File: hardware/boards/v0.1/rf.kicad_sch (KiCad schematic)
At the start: 12 parts, among them J1 WIFI_JTAG, SW22 BOOT, SW23 RST, U22 nRF, U27 ESP32-S3-MINI-1U, Y2 32.768kHz

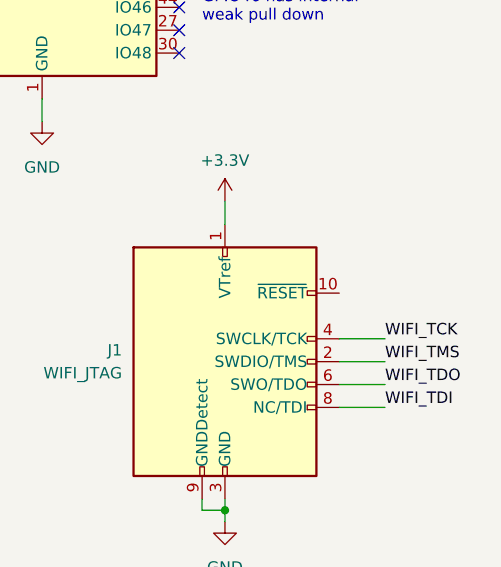
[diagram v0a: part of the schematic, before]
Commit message: feat: more routing and DRC cleanup
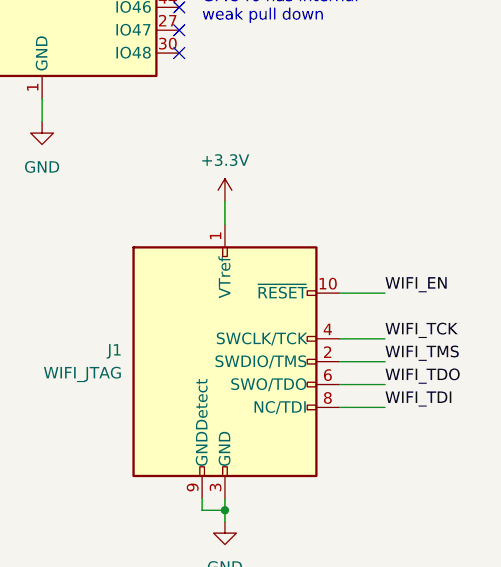
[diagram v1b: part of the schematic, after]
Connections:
- net ~{WIFI_EN}: now also J1.10 (~{RESET})
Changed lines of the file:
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@@
+	(wire
+		(pts
+			(xy 266.7 134.62) (xy 271.78 134.62)
+		)
+		(stroke
+			(width 0)
+			(type default)
+		)
+	)
 	(wire
 		(pts
@@
 		(effects
 			(font
+				(size 1.27 1.27)
+			)
+			(justify left bottom)
+		)
+	)
+	(label "WIFI_EN"
+		(at 271.78 134.62 0)
+		(effects
+			(font

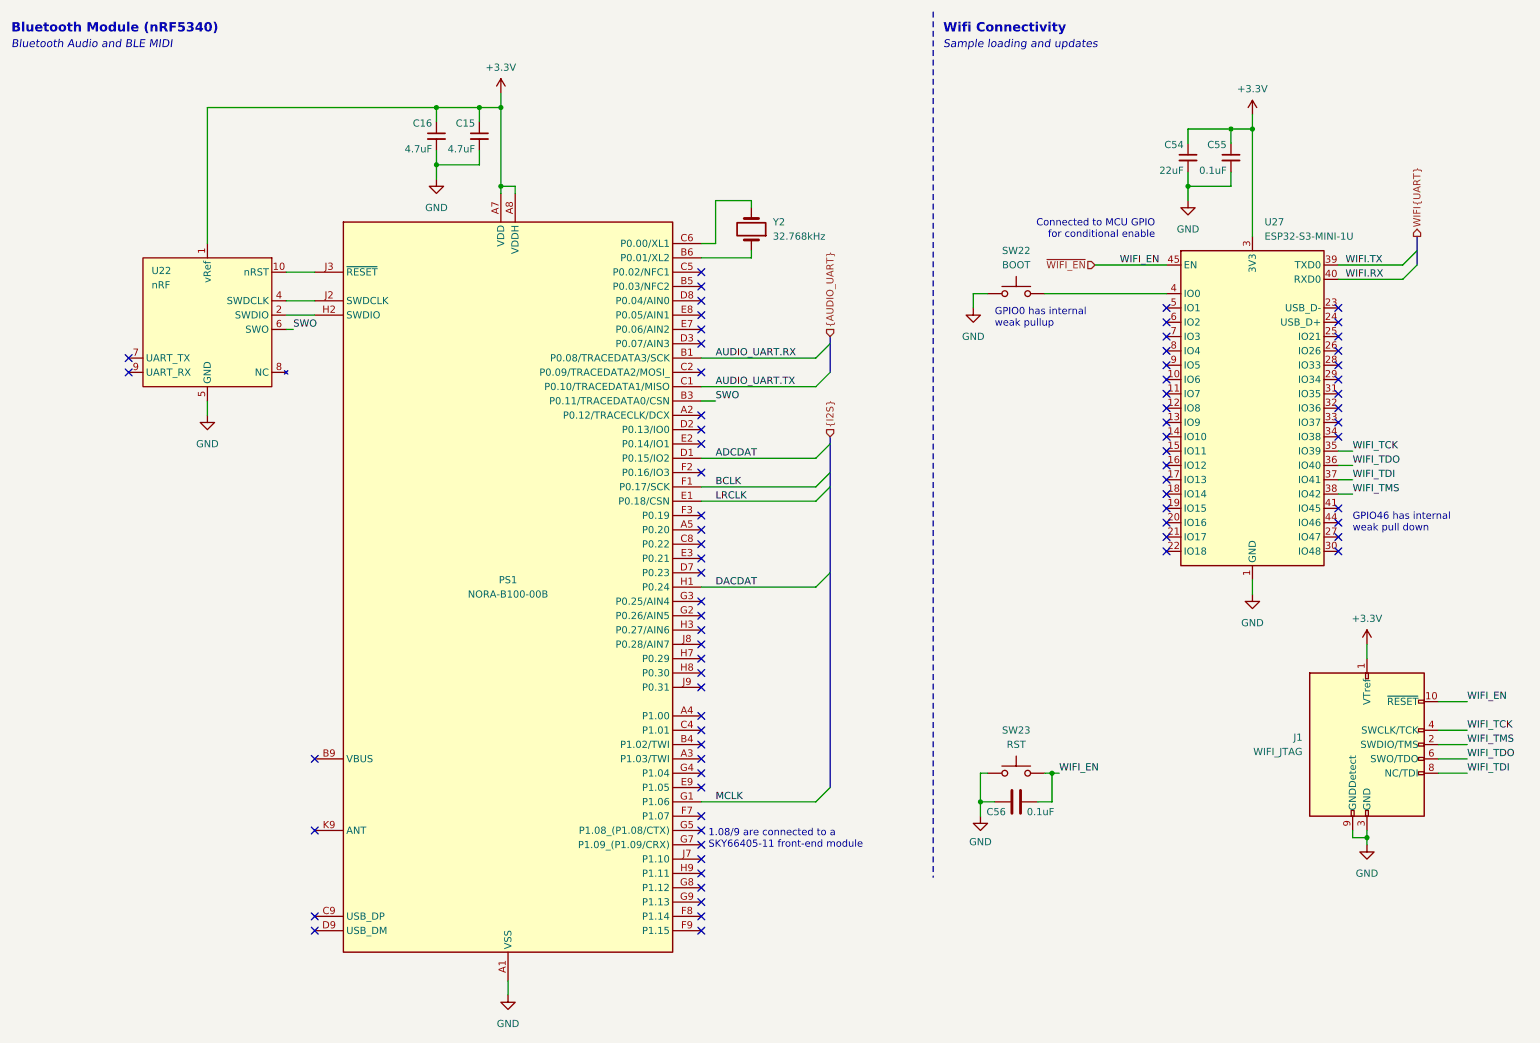
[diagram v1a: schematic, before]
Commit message: feat: clean up routing, remove metronome light
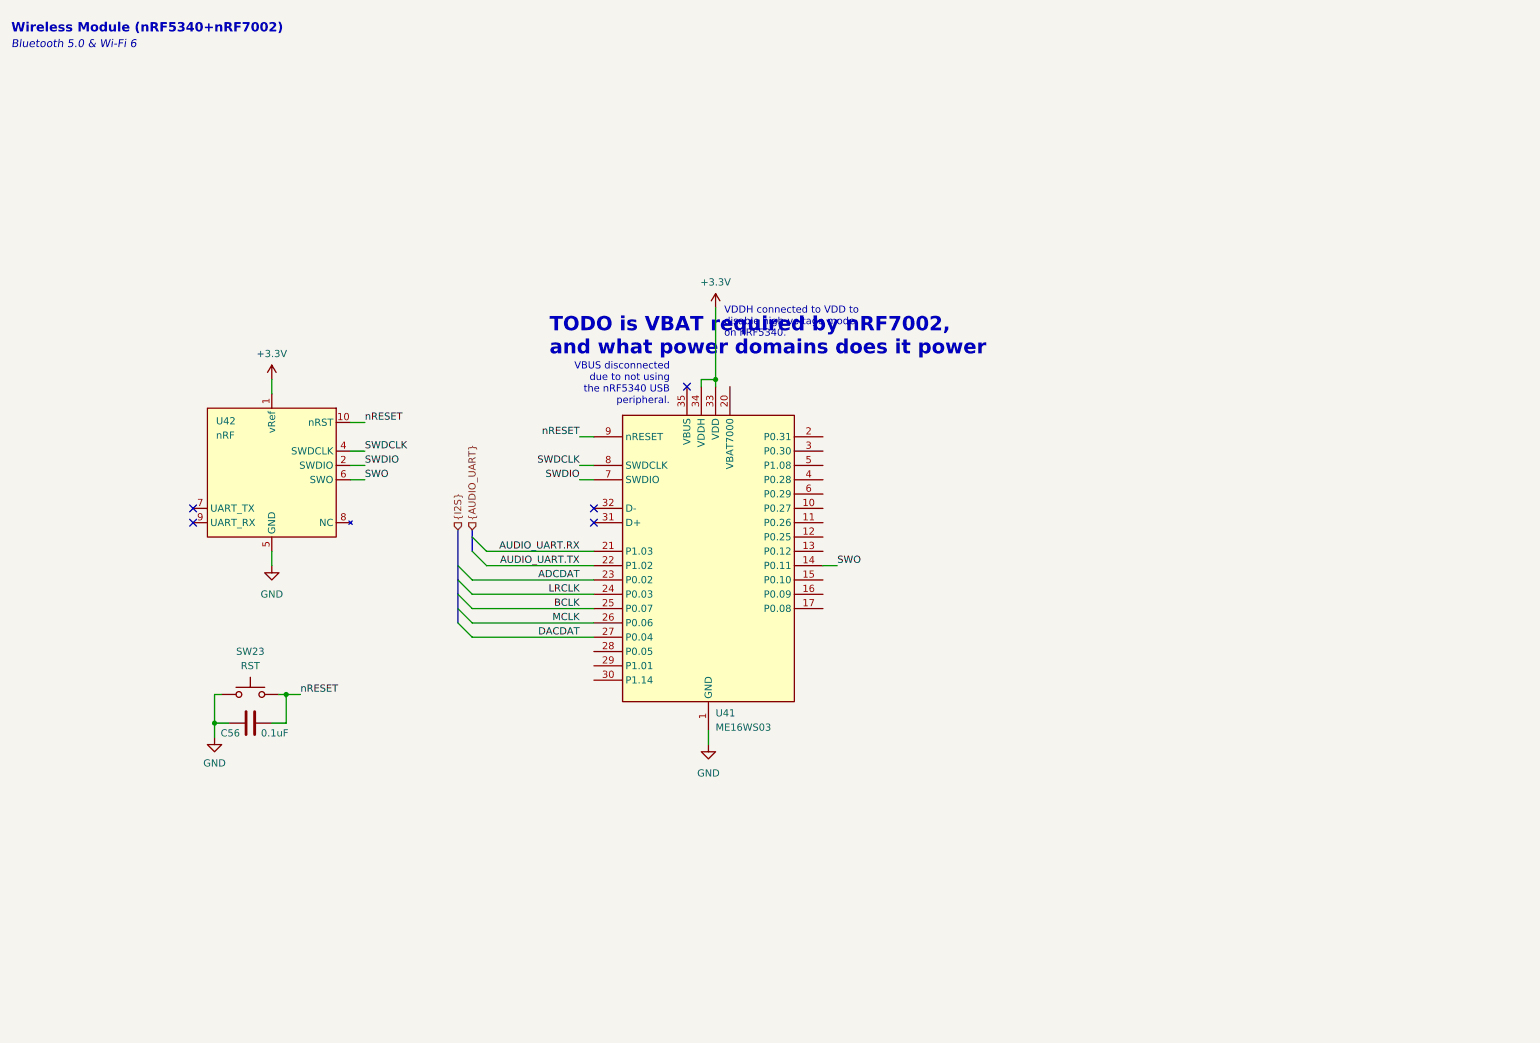
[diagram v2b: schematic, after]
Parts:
- removed C15, C16: 4.7uF, Capacitor_SMD:C_0402_1005Metric, symbol Device:C_Small
- removed C54: 22uF, Capacitor_SMD:C_0402_1005Metric, symbol Device:C_Small
- removed C55: 0.1uF, Capacitor_SMD:C_0402_1005Metric, symbol Device:C_Small
- removed J1: WIFI_JTAG, symbol Connector:Conn_ARM_JTAG_SWD_10
- removed PS1: NORA-B100-00B, pocket_synth:NORAB10000B, symbol pocket_synth:NORA-B100-00B
- removed SW22: BOOT, Button_Switch_SMD:SW_SPST_B3U-1000P, symbol Switch:SW_Push
- removed U22: nRF, pocket_synth:CON10_2X5_DUK_FTSH_SAI-M, symbol pocket_synth:BMDU
- removed U27: ESP32-S3-MINI-1U, RF_Module:ESP32-S2-MINI-1U, symbol RF_Module:ESP32-S3-MINI-1U
- removed Y2: 32.768kHz, symbol Device:Crystal
- added U41: ME16WS03, pocket_synth:ME16WS03, symbol pocket_synth:ME16WS03
- added U42: nRF, pocket_synth:CON10_2X5_DUK_FTSH_SAI-M, symbol pocket_synth:BMDU
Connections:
- net +3.3V: now also U41.33 (VDD), U41.34 (VDDH), U42.1 (vRef)
- net ADCDAT: now also U41.23 (P0.02)
- net AUDIO_UART.RX: now also U41.21 (P1.03)
- net AUDIO_UART.TX: now also U41.22 (P1.02)
- net BCLK: now also U41.25 (P0.07)
- net DACDAT: now also U41.27 (P0.04)
- net GND: now also U41.1 (GND), U41.18 (GND), U41.19 (GND), U41.36 (GND), U41.37 (GND), U41.38 (GND), U42.3 (GND), U42.5 (GND)
- net LRCLK: now also U41.24 (P0.03)
- net MCLK: now also U41.26 (P0.06)
- net SWO: now also U41.14 (P0.11), U42.6 (SWO)
- net ~{WIFI_EN} renamed nRESET
- net nRESET: now also U41.9 (nRESET), U42.10 (nRST)
- new net SWDCLK: U41.8 (SWDCLK), U42.4 (SWDCLK)
- new net SWDIO: U41.7 (SWDIO), U42.2 (SWDIO)
- no-connect marks 76 -> 5
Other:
- note added: "Bluetooth 5.0 & Wi-Fi 6"
- note added: "TODO is VBAT required by nRF7002, and what power domains does it power"
- note added: "VBUS disconnected due to not using the nRF5340 USB peripheral."
- note added: "VDDH connected to VDD to disable high-voltage mode on nRF5340."
- note added: "Wireless Module (nRF5340+nRF7002)"
- note removed: "1.08/9 are connected to a SKY66405-11 front-end module"
- note removed: "Bluetooth Audio and BLE MIDI"
- note removed: "Bluetooth Module (nRF5340)"
- note removed: "Connected to MCU GPIO for conditional enable"
- note removed: "GPIO0 has internal weak pullup"
- note removed: "GPIO46 has internal weak pull down"
- note removed: "Sample loading and updates"
- note removed: "Wifi Connectivity"
- moved on the sheet: C56, SW23

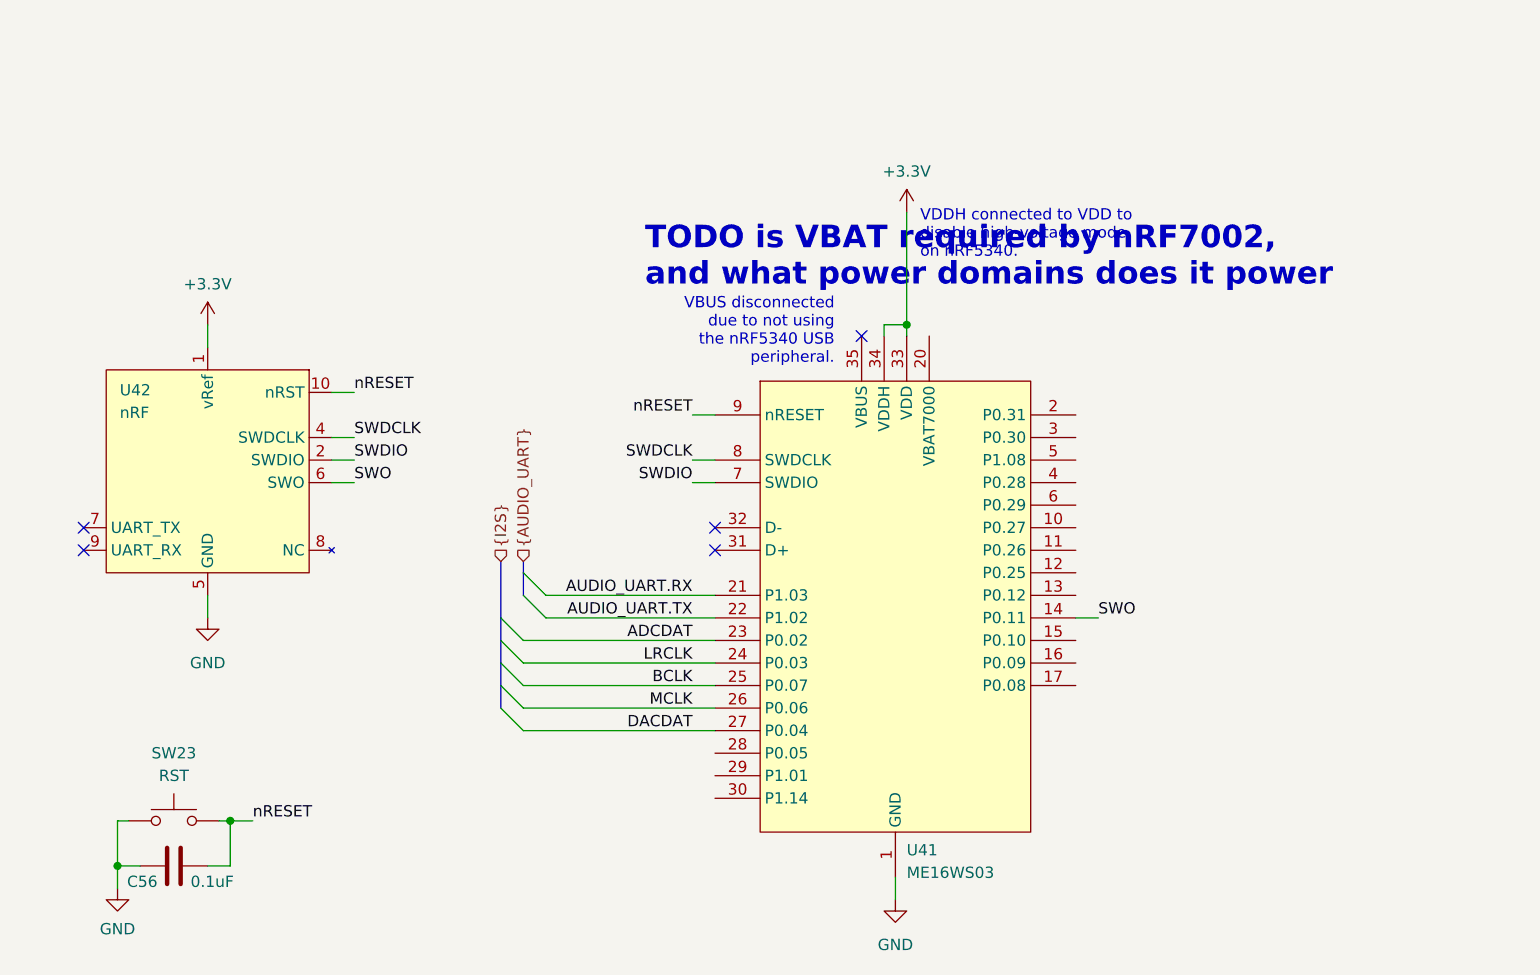
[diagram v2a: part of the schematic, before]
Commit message: feat: routing cleanup and start of BOM selection
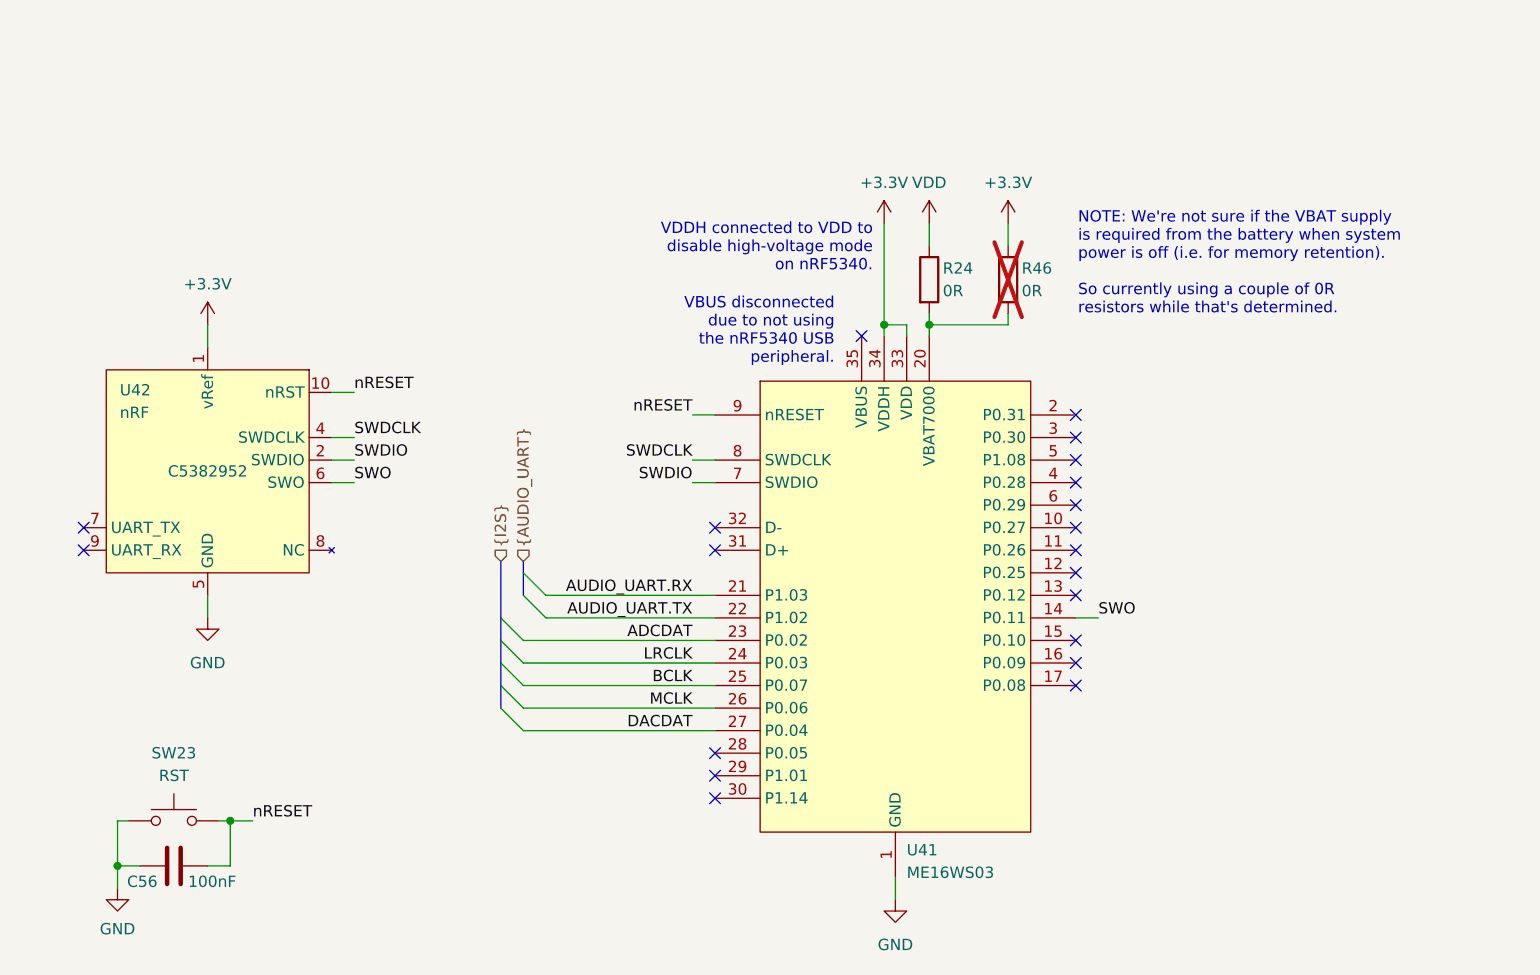
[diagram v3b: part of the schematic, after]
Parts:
- added R24, R46: 0R, Resistor_SMD:R_0603_1608Metric_Pad0.98x0.95mm_HandSolder, symbol Device:R
- C56: value 0.1uF -> 100nF; footprint (none) -> Capacitor_SMD:C_0603_1608Metric
- SW23: footprint (none) -> Button_Switch_SMD:SW_SPST_B3U-1000P; JLC (none) -> C231329
- U41: now left out of the parts list
- U42: JLC (none) -> C5382952
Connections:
- net +3.3V: now also R46.1
- net at U41.20 (VBAT7000): now also R24.2, R46.2
- new net VDD: R24.1
- no-connect marks 5 -> 20
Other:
- note added: "NOTE: We're not sure if the VBAT supply is required from the battery when system power is off (i.e. for memory retention). So currently using a couple of 0R resistors while that's determined."
- note removed: "TODO is VBAT required by nRF7002, and what power domains does it power"

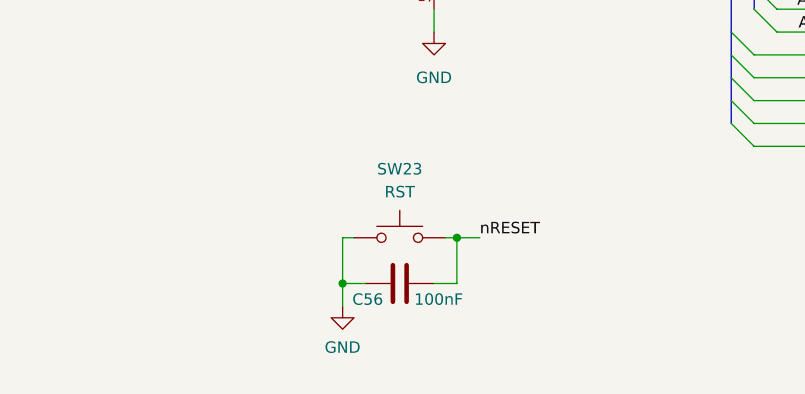
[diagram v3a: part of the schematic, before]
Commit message: feat: update various components to 0402
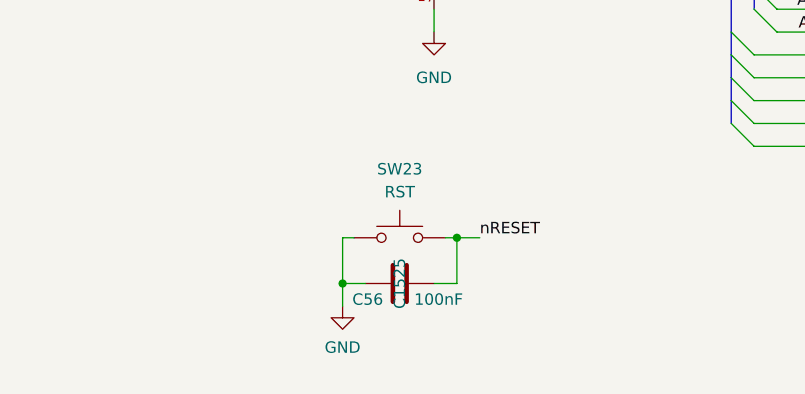
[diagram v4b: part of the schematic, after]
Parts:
- C56: JLC (none) -> C1525
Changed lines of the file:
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@@
+			)
+		)
+		(property "JLC" "C1525"
+			(at 55.88 138.43 0)
+			(effects
+				(font
+					(size 1.27 1.27)
+				)
 			)
 		)
@@
 			)
 		)
-		(property "Arrow Part Number" ""
-			(at 59.69 93.98 0)
-			(effects
-				(font
-					(size 1.27 1.27)
-				)
-			)
-		)
-		(property "Arrow Price/Stock" ""
-			(at 59.69 93.98 0)
-			(effects
-				(font
-					(size 1.27 1.27)
-				)
-			)
-		)
 		(property "MANUFACTURER" ""
 			(at 59.69 93.98 0)
@@
 			(at 59.69 93.98 0)
 			(effects
-				(font
-					(size 1.27 1.27)
-				)
-			)
-		)
-		(property "PARTREV" ""
-			(at 59.69 93.98 0)
-			(effects
-				(font
-					(size 1.27 1.27)
-				)
-			)
-		)
-		(property "STANDARD" ""
-			(at 59.69 93.98 0)
-			(effects
